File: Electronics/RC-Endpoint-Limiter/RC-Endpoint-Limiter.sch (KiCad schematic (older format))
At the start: 44 parts, among them J1 USB_B_Micro, J2 Aux Low, J3 Aux High, J4 Switch Low, J5 Switch High, J6 RC Input, J7 RC Output, J8 Inhibit Input, U1 ATmega32U4-MU, Y1 8Mhz

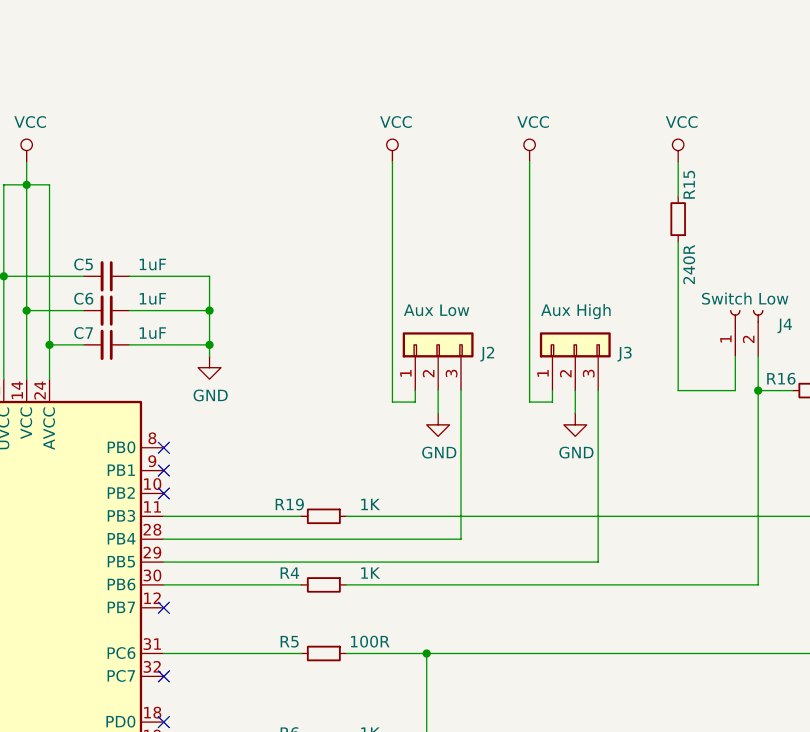
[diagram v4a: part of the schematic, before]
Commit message: made aux inputs dedicated hall inputs, Make sure to enable pullups,  bit low on board space around there to fit external pullup resistors added fuses.
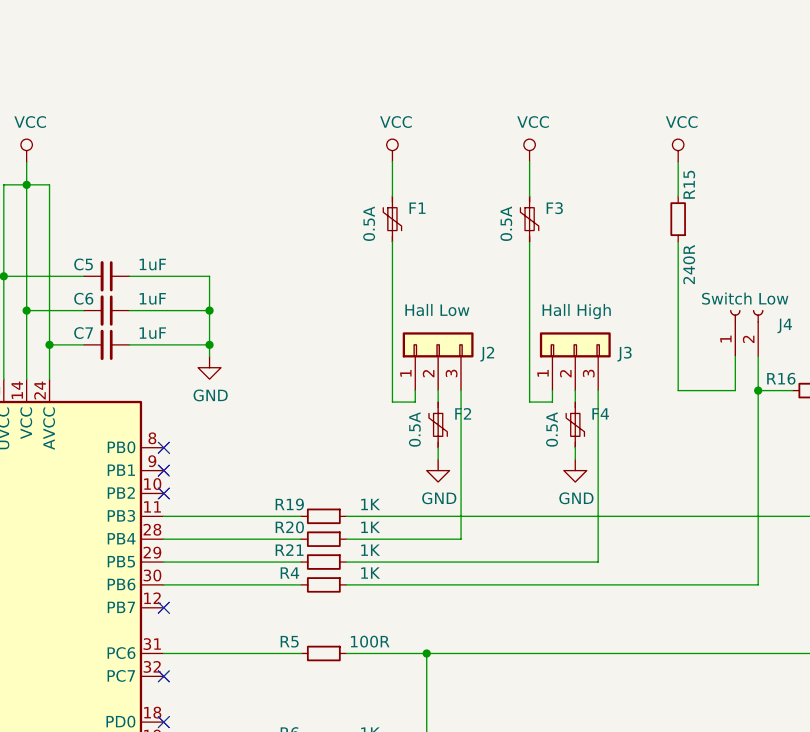
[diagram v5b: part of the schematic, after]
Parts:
- added F1, F2, F3, F4: 0.5A, Fuse:Fuse_0603_1608Metric, symbol Device:Polyfuse_Small
- added R20, R21: 1K, Resistor_SMD:R_0603_1608Metric, symbol Device:R_Small
- J2: value Aux Low -> Hall Low
- J3: value Aux High -> Hall High
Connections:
- net GND: now also F2.2, F4.2; no longer J2.2 (Pin_2), J3.2 (Pin_2)
- net VCC: now also F1.1, F3.1; no longer J2.1 (Pin_1), J3.1 (Pin_1)
- net at U1.28 (PB4): now also R20.2; no longer J2.3 (Pin_3)
- net at U1.29 (PB5): now also R21.2; no longer J3.3 (Pin_3)
- new net: F1.2, J2.1 (Pin_1)
- new net: F2.1, J2.2 (Pin_2)
- new net: J2.3 (Pin_3), R20.1
- new net: F3.2, J3.1 (Pin_1)
- new net: F4.1, J3.2 (Pin_2)
- new net: J3.3 (Pin_3), R21.1
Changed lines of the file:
@@
 P 6050 2450
 F 0 "J2" V 6014 2262 50  0000 R CNN
-F 1 "Aux Low" V 6200 2600 50  0000 R CNN
+F 1 "Hall Low" V 6200 2600 50  0000 R CNN
 F 2 "Connector_PinHeader_1.27mm:PinHeader_1x03_P1.27mm_Horizontal" H 6050 2450 50  0001 C CNN
 F 3 "~" H 6050 2450 50  0001 C CNN
@@
 P 6650 2450
 F 0 "J3" V 6614 2262 50  0000 R CNN
-F 1 "Aux High" V 6800 2600 50  0000 R CNN
+F 1 "Hall High" V 6800 2600 50  0000 R CNN
 F 2 "Connector_PinHeader_1.27mm:PinHeader_1x03_P1.27mm_Horizontal" H 6650 2450 50  0001 C CNN
 F 3 "~" H 6650 2450 50  0001 C CNN
@@
 L power:GND #PWR011
 U 1 1 5D8379C3
-P 6050 2750
-F 0 "#PWR011" H 6050 2500 50  0001 C CNN
-F 1 "GND" H 6055 2577 50  0000 C CNN
-F 2 "" H 6050 2750 50  0001 C CNN
-F 3 "" H 6050 2750 50  0001 C CNN
-	1    6050 2750
+P 6050 2950
+F 0 "#PWR011" H 6050 2700 50  0001 C CNN
+F 1 "GND" H 6055 2777 50  0000 C CNN
+F 2 "" H 6050 2950 50  0001 C CNN
+F 3 "" H 6050 2950 50  0001 C CNN
+	1    6050 2950
 	1    0    0    -1
 $EndComp
@@
 	5950 2700 5950 2650
 Wire Wire Line
-	6050 2750 6050 2650
-Wire Wire Line
-	4850 3300 6150 3300
+	4850 3300 5450 3300
 Wire Wire Line
 	6150 3300 6150 2650
 Wire Wire Line
-	4850 3400 6750 3400
+	4850 3400 5450 3400
 Wire Wire Line
 	6750 3400 6750 2650
@@
 L power:GND #PWR015
 U 1 1 5D84E821
-P 6650 2750
-F 0 "#PWR015" H 6650 2500 50  0001 C CNN
-F 1 "GND" H 6655 2577 50  0000 C CNN
-F 2 "" H 6650 2750 50  0001 C CNN
-F 3 "" H 6650 2750 50  0001 C CNN
-	1    6650 2750
-	1    0    0    -1
-$EndComp
-Wire Wire Line
-	6650 2650 6650 2750
+P 6650 2950
+F 0 "#PWR015" H 6650 2700 50  0001 C CNN
+F 1 "GND" H 6655 2777 50  0000 C CNN
+F 2 "" H 6650 2950 50  0001 C CNN
+F 3 "" H 6650 2950 50  0001 C CNN
+	1    6650 2950
+	1    0    0    -1
+$EndComp
+Wire Wire Line
+	6650 2650 6650 2700
 $Comp
 L power:VCC #PWR012
@@
 	6550 2700 6450 2700
 Wire Wire Line
-	5850 1650 5850 2700
-Wire Wire Line
-	6450 1650 6450 2700
+	6450 1650 6450 1800
 Wire Wire Line
 	4850 3500 5450 3500
@@
 Wire Wire Line
 	11050 3200 11050 2650
+Wire Wire Line
+	6450 2000 6450 2700
+Wire Wire Line
+	5850 1650 5850 1800
+Wire Wire Line
+	5850 2000 5850 2700
+$Comp
+L Device:Polyfuse_Small F2
+U 1 1 5D82754C
+P 6050 2800
+F 0 "F2" H 6118 2846 50  0000 L CNN
+F 1 "0.5A" V 5950 2700 50  0000 L CNN
+F 2 "Fuse:Fuse_0603_1608Metric" H 6100 2600 50  0001 L CNN
+F 3 "~" H 6050 2800 50  0001 C CNN
+	1    6050 2800
+	1    0    0    -1
+$EndComp
+Wire Wire Line
+	6050 2700 6050 2650
+Wire Wire Line
+	6050 2900 6050 2950
+Wire Wire Line
+	6650 2900 6650 2950
+$Comp
+L Device:Polyfuse_Small F4
+U 1 1 5D8547FF
+P 6650 2800
+F 0 "F4" H 6718 2846 50  0000 L CNN
+F 1 "0.5A" V 6550 2700 50  0000 L CNN
+F 2 "Fuse:Fuse_0603_1608Metric" H 6700 2600 50  0001 L CNN
+F 3 "~" H 6650 2800 50  0001 C CNN
+	1    6650 2800
+	1    0    0    -1
+$EndComp
+$Comp
+L Device:Polyfuse_Small F3
+U 1 1 5D854CA3
+P 6450 1900
+F 0 "F3" H 6518 1946 50  0000 L CNN
+F 1 "0.5A" V 6350 1800 50  0000 L CNN
+F 2 "Fuse:Fuse_0603_1608Metric" H 6500 1700 50  0001 L CNN
+F 3 "~" H 6450 1900 50  0001 C CNN
+	1    6450 1900
+	1    0    0    -1
+$EndComp
+$Comp
+L Device:Polyfuse_Small F1
+U 1 1 5D855279
+P 5850 1900
+F 0 "F1" H 5918 1946 50  0000 L CNN
+F 1 "0.5A" V 5750 1800 50  0000 L CNN
+F 2 "Fuse:Fuse_0603_1608Metric" H 5900 1700 50  0001 L CNN
+F 3 "~" H 5850 1900 50  0001 C CNN
+	1    5850 1900
+	1    0    0    -1
+$EndComp
+$Comp
+L Device:R_Small R20
+U 1 1 5D858144
+P 5550 3300
+F 0 "R20" V 5500 3150 50  0000 C CNN
+F 1 "1K" V 5500 3500 50  0000 C CNN
+F 2 "Resistor_SMD:R_0603_1608Metric" H 5550 3300 50  0001 C CNN
+F 3 "~" H 5550 3300 50  0001 C CNN
+	1    5550 3300
+	0    1    1    0
+$EndComp
+Wire Wire Line
+	5650 3300 6150 3300
+$Comp
+L Device:R_Small R21
+U 1 1 5D858502
+P 5550 3400
+F 0 "R21" V 5500 3250 50  0000 C CNN
+F 1 "1K" V 5500 3600 50  0000 C CNN
+F 2 "Resistor_SMD:R_0603_1608Metric" H 5550 3400 50  0001 C CNN
+F 3 "~" H 5550 3400 50  0001 C CNN
+	1    5550 3400
+	0    1    1    0
+$EndComp
+Wire Wire Line
+	5650 3400 6750 3400
 $EndSCHEMATC

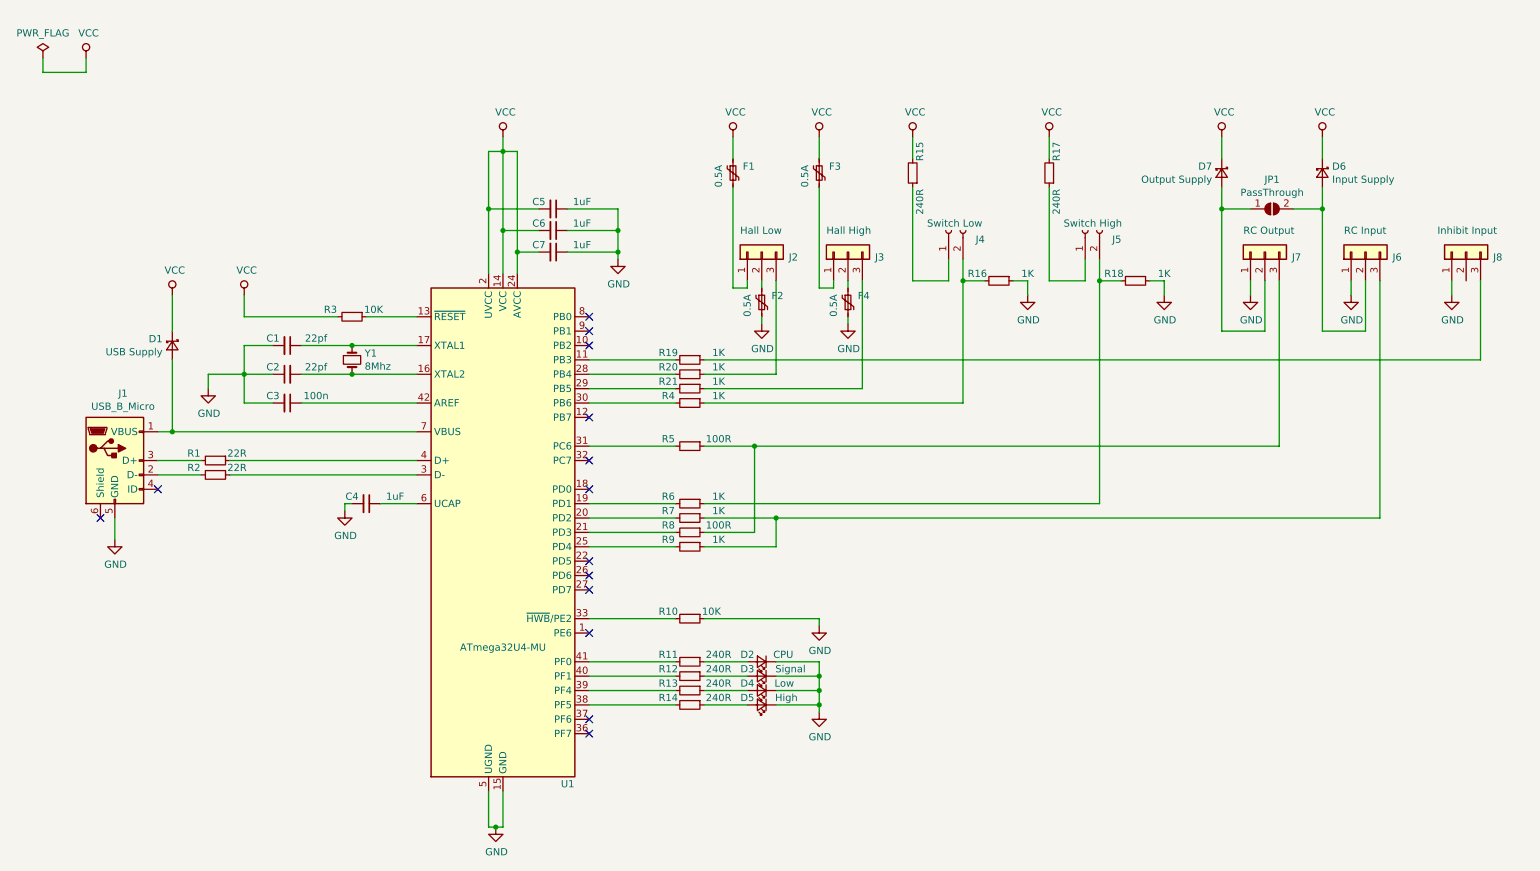
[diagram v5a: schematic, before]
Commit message: added lots more I/O
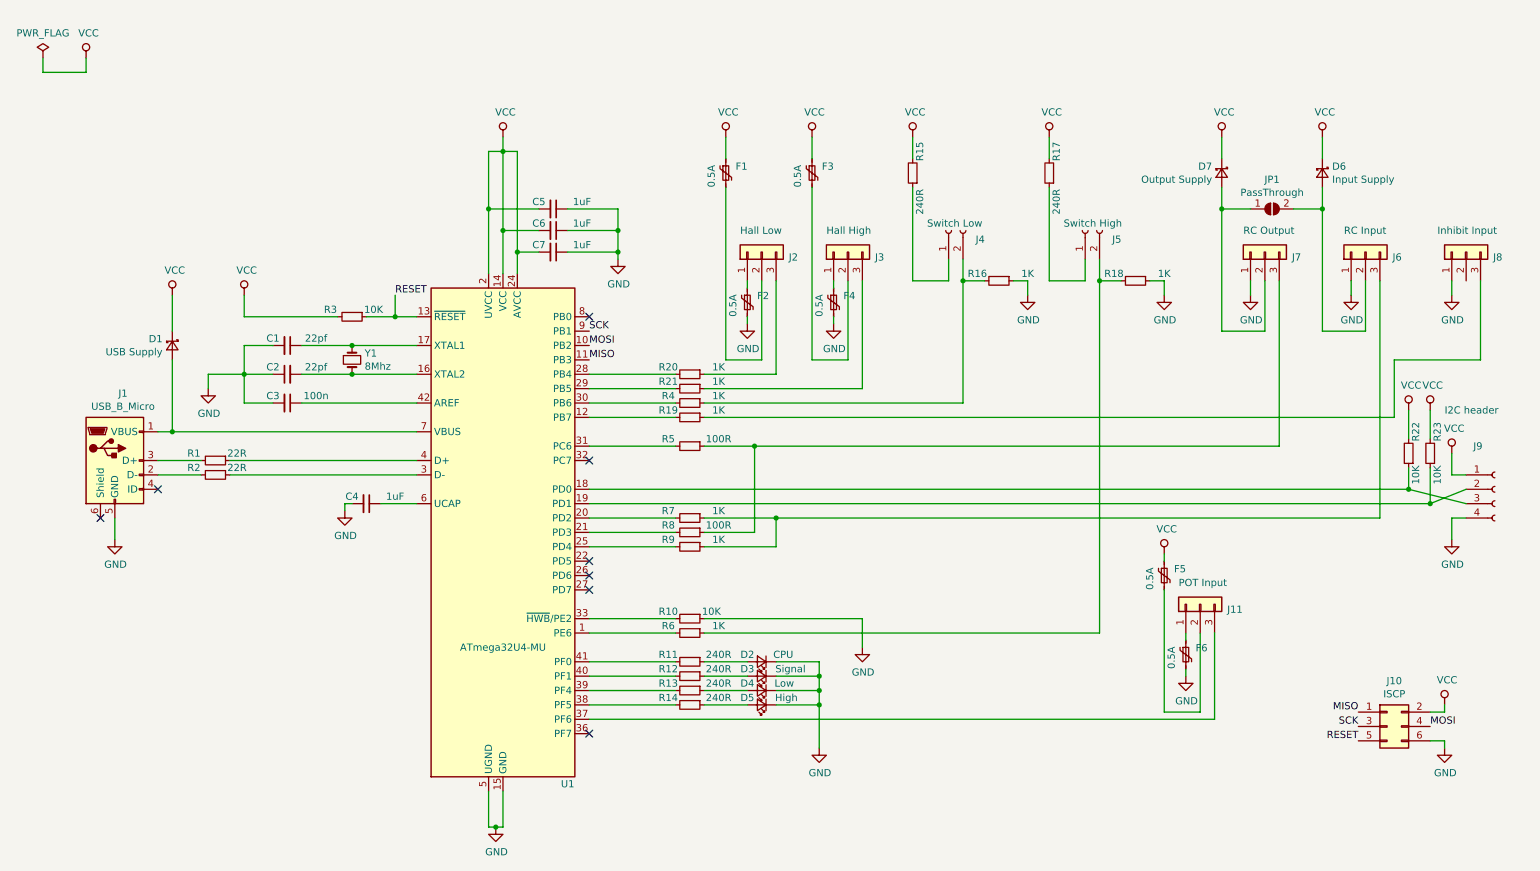
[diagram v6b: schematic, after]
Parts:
- added F5, F6: 0.5A, Fuse:Fuse_0603_1608Metric, symbol Device:Polyfuse_Small
- added J10: ISCP, Connector_PinHeader_1.27mm:PinHeader_2x03_P1.27mm_Vertical, symbol Connector_Generic:Conn_02x03_Odd_Even
- added J11: POT Input, Connector_PinHeader_1.27mm:PinHeader_1x03_P1.27mm_Horizontal, symbol Connector_Generic:Conn_01x03
- added J9: I2C header, Connector_PinHeader_1.27mm:PinHeader_1x04_P1.27mm_Horizontal, symbol Connector:Conn_01x04_Female
- added R22, R23: 10K, Resistor_SMD:R_0603_1608Metric, symbol Device:R_Small
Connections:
- net GND: now also F6.2, J10.6 (Pin_6), J9.4 (Pin_4)
- net VCC: now also F5.1, J10.2 (Pin_2), J9.1 (Pin_1), R22.2, R23.2
- net RESET: now reaches R3.1, U1.13 (~RESET)
- net RESET: now also J10.5 (Pin_5)
- net at U1.1 (PE6): now also R6.2
- net MOSI: now reaches U1.10 (PB2)
- net MOSI: now also J10.4 (Pin_4)
- net at R19.2: now also U1.12 (PB7); no longer U1.11 (PB3)
- net at U1.18 (PD0): now also J9.3 (Pin_3), R22.1
- net at U1.19 (PD1): now also J9.2 (Pin_2), R23.1; no longer R6.2
- net at U1.37 (PF6): now also J11.3 (Pin_3)
- net SCK: now reaches U1.9 (PB1)
- net SCK: now also J10.3 (Pin_3)
- net at J2.1 (Pin_1): now also F2.1; no longer F1.2
- net at J2.2 (Pin_2): now also F1.2; no longer F2.1
- net at J3.1 (Pin_1): now also F4.1; no longer F3.2
- net at J3.2 (Pin_2): now also F3.2; no longer F4.1
- new net: F6.1, J11.1 (Pin_1)
- new net: F5.2, J11.2 (Pin_2)
- new net MISO: J10.1 (Pin_1), U1.11 (PB3)
- no-connect marks 14 -> 8
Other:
- moved on the sheet: F1, F2, F3, F4, R19, R6

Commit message: polished up PCB layout
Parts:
- added R24: 1K, Resistor_SMD:R_0603_1608Metric, symbol Device:R_Small
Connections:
- net at U1.37 (PF6): now also R24.2; no longer J11.3 (Pin_3)
- new net: J11.3 (Pin_3), R24.1
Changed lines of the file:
@@
 	6450 5600 6450 5900
 Wire Wire Line
-	4850 5700 9200 5700
+	4850 5700 5450 5700
 Wire Wire Line
 	9200 5700 9200 5100
 Wire Wire Line
 	8850 4550 8850 4600
+$Comp
+L Device:R_Small R24
+U 1 1 5DAC9E36
+P 5550 5700
+F 0 "R24" V 5500 5550 50  0000 C CNN
+F 1 "1K" V 5500 5900 50  0000 C CNN
+F 2 "Resistor_SMD:R_0603_1608Metric" H 5550 5700 50  0001 C CNN
+F 3 "~" H 5550 5700 50  0001 C CNN
+	1    5550 5700
+	0    1    1    0
+$EndComp
+Wire Wire Line
+	5650 5700 9200 5700
 $EndSCHEMATC
